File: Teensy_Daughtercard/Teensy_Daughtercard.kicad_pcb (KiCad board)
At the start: 4 copper layers, 100 x 100 mm, 12 parts, among them J1 XG4A-5034, J6 LPJ4012AHNL, U1 Teensy4.1

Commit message: First draft complete
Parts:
- removed the H1 at (107.2, 135.9)
- removed H4: MH, MountingHole:MountingHole_3.5mm_Pad
- moved TP2 92.9 mm to (107.0, 98.0)
- moved TP1 77.7 mm to (117.8, 69.8)
- moved TP3 73.3 mm to (122.8, 69.8)
- moved G*** 69.0 mm to (168.1, 61.4), turned to 0 degrees
- moved H1 14.1 mm to (107.2, 60.0)
- moved H2 14.1 mm to (197.2, 60.0)
- moved C1 14.1 mm to (140.5, 73.4)
- moved J1 14.1 mm to (156.6, 74.4)
- renumbered H2 to H1, H3 to H2, J6 to J1, J1 to J6
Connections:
- net ENA1 renamed /RELAY1
- net RELAY10 renamed /GPIO4
- J6 pad 1: RELAY16 -> /RELAY15
- J6 pad 10: RELAY5 -> /RELAY3
- J6 pad 12: RELAY1 -> /ENA1
- J6 pad 13: PUL4 -> /DIR4
- J6 pad 14: DIR4 -> /PUL4
- J6 pad 15: DIR2 -> /ENA3
- J6 pad 16: ENA3 -> /DIR2
- J6 pad 17: SCLLC -> /PUL2
- J6 pad 18: PUL2 -> /SCLLC
- J6 pad 19: VMC+ -> +5V
- J6 pad 2: RELAY15 -> /RELAY16
- J6 pad 20: +5V -> VMC+
- J6 pad 21: SCLTC -> GNDD
- J6 pad 22: GNDD -> /SCLTC
- J6 pad 23: SDO1 -> /SDATC
- J6 pad 24: SDATC -> /SDO1
- J6 pad 25: Imon PS1 -> /SDI1
- J6 pad 26: SDI1 -> /Imon PS1
- J6 pad 27: GPIO1 -> /Imon PS2
- J6 pad 28: Imon PS2 -> /GPIO1
- J6 pad 29: GPIO3 -> /GPIO2
- J6 pad 3: RELAY13 -> /RELAY14
- J6 pad 30: GPIO2 -> /GPIO3
- J6 pad 32: GPIO4 -> /RELAY10
- J6 pad 33: RELAY6 -> /RELAY7
- J6 pad 34: RELAY7 -> /RELAY6
- J6 pad 35: RELAY2 -> /RELAY4
- J6 pad 36: RELAY4 -> /RELAY2
- J6 pad 37: PUL1 -> /DIR1
- J6 pad 38: DIR1 -> /PUL1
- J6 pad 39: DIR3 -> /ENA4
- J6 pad 4: RELAY14 -> /RELAY13
- J6 pad 40: ENA4 -> /DIR3
- J6 pad 41: ENA2 -> /PUL3
- J6 pad 42: PUL3 -> /ENA2
- J6 pad 43: +5V -> /SDALC
- J6 pad 44: SDALC -> +5V
- J6 pad 45: GNDD -> VMC+
- J6 pad 46: VMC+ -> GNDD
- J6 pad 49: SCLK1 -> /CS1
- J6 pad 5: RELAY11 -> /RELAY12
- J6 pad 50: CS1 -> /SCLK1
- J6 pad 6: RELAY12 -> /RELAY11
- J6 pad 7: RELAY8 -> /RELAY9
- J6 pad 8: RELAY9 -> /RELAY8
- J6 pad 9: RELAY3 -> /RELAY5
- U1 pad 10: GPIO2 -> /RELAY10
- U1 pad 11: GPIO3 -> /RELAY9
- U1 pad 12: CS1 -> /CS1
- U1 pad 13: SDI1 -> /SDI1
- U1 pad 14: SDO1 -> /SDO1
- U1 pad 16: Imon PS2 -> /RELAY7
- U1 pad 17: Imon PS1 -> /RELAY8
- U1 pad 18: PUL2 -> /RELAY6
- U1 pad 19: DIR2 -> /RELAY5
- U1 pad 2: PUL1 -> /GPIO1
- U1 pad 20: ENA3 -> /RELAY4
- U1 pad 21: PUL4 -> /RELAY3
- U1 pad 22: DIR4 -> /RELAY2
- U1 pad 24: RELAY1 -> /DIR1
- U1 pad 25: RELAY3 -> /DIR4
- U1 pad 26: RELAY5 -> /PUL1
- U1 pad 27: RELAY8 -> /ENA1
- U1 pad 28: RELAY9 -> /ENA4
- U1 pad 29: RELAY11 -> /PUL4
- U1 pad 3: DIR1 -> /RELAY14
- U1 pad 30: RELAY12 -> /DIR3
- U1 pad 31: RELAY13 -> /ENA3
- U1 pad 32: RELAY14 -> /PUL3
- U1 pad 33: RELAY16 -> /DIR2
- U1 pad 35: SCLK1 -> /SCLK1
- U1 pad 36: RELAY15 -> /PUL2
- U1 pad 37: GPIO1 -> /ENA2
- U1 pad 38: SCLLC -> /SCLLC
- U1 pad 39: SDALC -> /SDALC
- U1 pad 4: RELAY2 -> /GPIO2
- U1 pad 40: SCLTC -> /SDATC
- U1 pad 41: SDATC -> /SCLTC
- U1 pad 42: ENA2 -> /RELAY16
- U1 pad 43: PUL3 -> /RELAY15
- U1 pad 44: DIR3 -> /Imon PS2
- U1 pad 45: ENA4 -> /Imon PS1
- U1 pad 5: RELAY4 -> /RELAY13
- U1 pad 6: RELAY6 -> /GPIO3
- U1 pad 7: RELAY7 -> /RELAY12
- U1 pad 9: GPIO4 -> /RELAY11
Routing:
- net /PUL2: track 0.00 -> 145.8 mm, vias 0 -> 1
- net /ENA2: track 0.00 -> 145.2 mm, vias 0 -> 1
- net /SCLLC: track 0.00 -> 138.9 mm, vias 0 -> 1
- net /SDALC: track 0.00 -> 138.8 mm, vias 0 -> 1
- net SCLLC: track 126.3 -> 0.00 mm, vias 2 -> 0
- net /SCLTC: track 0.00 -> 124.6 mm
- net +5V: track 0.00 -> 120.5 mm
- net SCLTC: track 120.4 -> 0.00 mm
- net /SDATC: track 0.00 -> 116.0 mm
- net CS1: track 110.9 -> 0.00 mm, vias 2 -> 0
- net SDATC: track 109.4 -> 0.00 mm
- net SCLK1: track 98.2 -> 0.00 mm
- net /DIR2: track 0.00 -> 95.7 mm
- net SDALC: track 92.9 -> 0.00 mm
- net RELAY15: track 92.2 -> 0.00 mm, vias 2 -> 0
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- added copper zone on B.Cu, net GNDD
- removed copper zone on B.Cu, net +5V
- removed copper zone on In1.Cu, net GNDD
- removed copper zone on In2.Cu, net GNDD
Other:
- board size 100 x 100 mm -> 100 x 88 mm
- copper layers 4 -> 2
- board text added: "Teensy4.1 Daughtercard v1.0"
- board text removed: "Teensy4.1 Daughtercard for the GigaPCB v2.0"

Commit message: First revision 6/11
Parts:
- added 3v3: LTST-C190YKT, LIST-C190YKT:LEDC1608X90N, F.Cu at (122.8, 75.0)
- added R1: 500, Resistor_SMD:R_0805_2012Metric_Pad1.20x1.40mm_HandSolder, F.Cu at (118.4, 75.0)
- moved TP2 14.2 mm to (119.2, 90.8)
- moved C1 2.98 mm to (140.4, 70.4)
- moved J1 1.89 mm to (156.3, 72.5)
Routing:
- net +5V: track 120.5 -> 77.9 mm
- net /RELAY16: track 89.1 -> 102.7 mm
- net /ETH_TX-: track 33.2 -> 45.1 mm, vias 1 -> 0
- net /ETH_RX+: track 26.3 -> 37.6 mm
- net /RELAY15: track 80.3 -> 91.2 mm
- net /ETH_RX-: track 26.6 -> 37.4 mm
- net /ETH_TX+: track 34.5 -> 44.5 mm, vias 1 -> 0
- net /ETH_LED: track 42.7 -> 46.0 mm, vias 3 -> 0
- net Net-(LED1-A): track 0.00 -> 2.60 mm
- net /Imon PS2: track 77.1 -> 78.9 mm
- net Net-(J1-RCT): track 16.9 -> 16.2 mm
- net /Imon PS1: track 67.2 -> 66.5 mm
- net GNDD: vias 2 -> 144
- net VMC+: vias 12 -> 2
- added copper zone on In1.Cu, net GNDD
- added copper zone on In2.Cu, net VMC+
- removed copper zone on B.Cu, net GNDD
- removed copper zone on F.Cu, net VMC+
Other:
- copper layers 2 -> 4

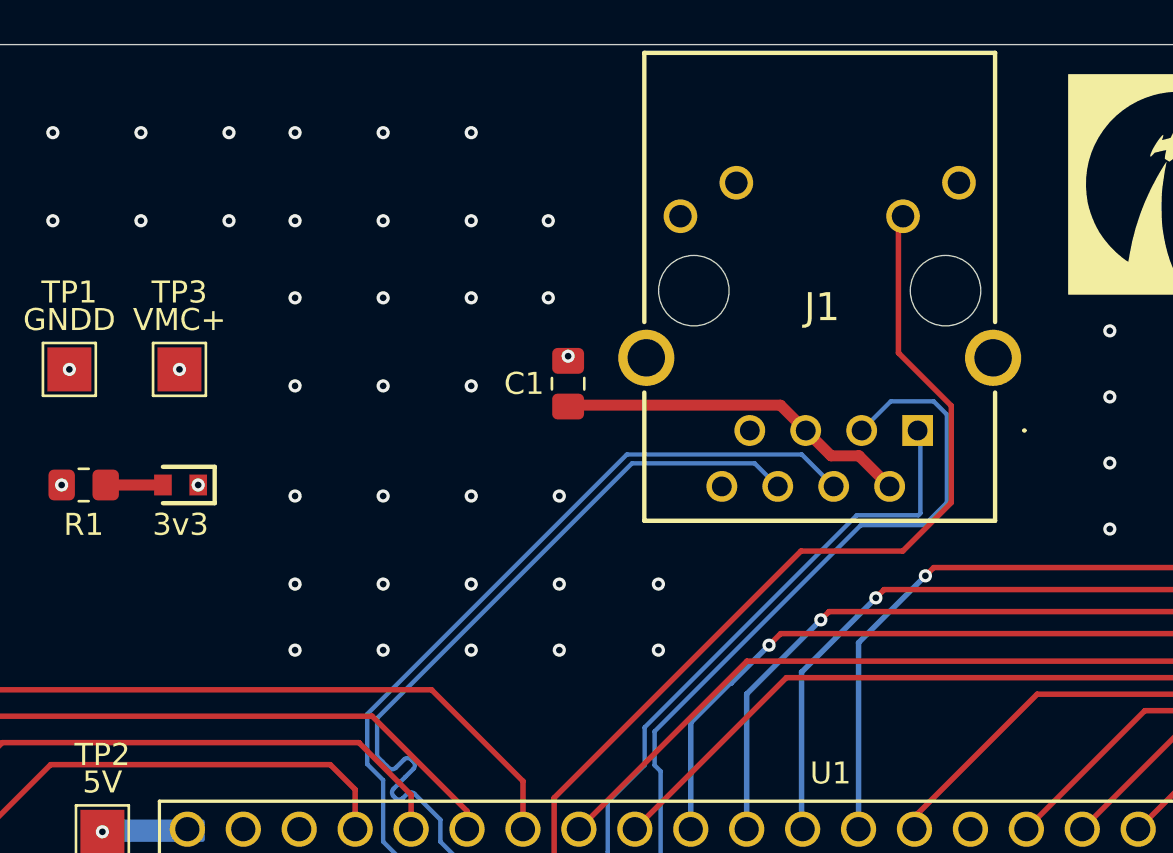
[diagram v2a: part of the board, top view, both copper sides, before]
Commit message: Replaced Magjack
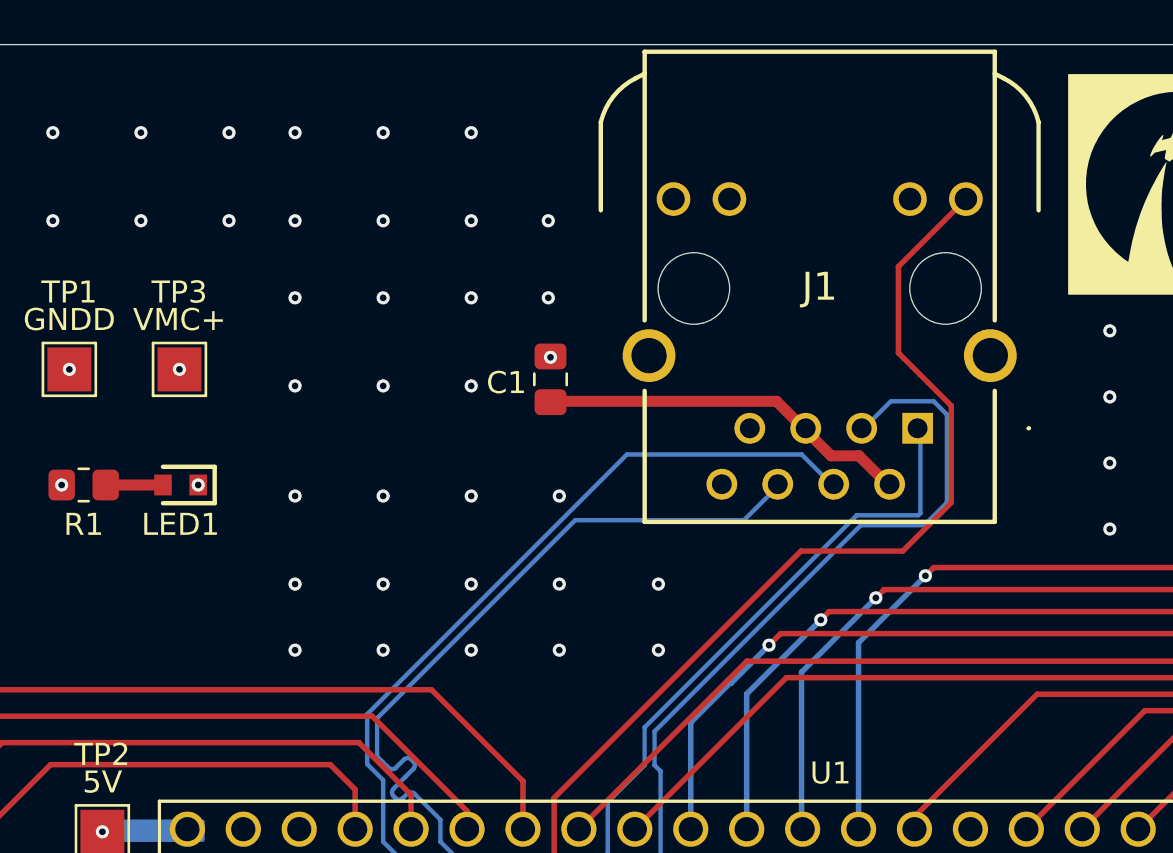
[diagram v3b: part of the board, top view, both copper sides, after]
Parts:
- J1: value LPJ4012AHNL -> 1664073; footprint LPJ4012AHNL:LPJ4012AHNL -> 1664073:1664073
- moved C1 0.82 mm to (139.6, 70.2)
- moved J1 0.10 mm to (156.3, 72.4)
- renumbered 3v3 to LED1
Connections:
- J1 pad 1: /ETH_TX+ -> unconnected-(J1-MH1-Pad1)
- J1 pad 2: Net-(J1-RCT) -> unconnected-(J1-MH2-Pad2)
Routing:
- net /ETH_LED: track 46.0 -> 48.0 mm
- net /ETH_RX-: track 37.4 -> 36.5 mm
- net Net-(J1-RCT): track 16.2 -> 17.0 mm

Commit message: Final changes
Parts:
- R1: value 500 -> 1000
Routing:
- net /SCLK1: track 89.5 -> 69.4 mm
- net /SDO1: track 64.5 -> 67.9 mm, vias 1 -> 0
- net +5V: track 77.9 -> 76.1 mm
- net /CS1: track 68.9 -> 70.4 mm, vias 1 -> 0
- net /SDI1: track 70.4 -> 71.3 mm, vias 3 -> 0
- net GNDD: vias 144 -> 145
